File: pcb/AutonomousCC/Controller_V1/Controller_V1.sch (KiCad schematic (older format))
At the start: 7 parts, among them J1 Antenna_Conn_02x04_Odd_Even, U1 COM-09032, U2 Pico, U3 COM-09032

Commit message: Added USB Port, Button, LED
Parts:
- added D?: Red_LED, symbol Device:LED
- added D?: Green_LED, symbol Device:LED
- added J?: USB1130-15-A_REVA, GCT_USB1130-15-A_REVA, symbol USB1130-15-A_REVA:USB1130-15-A_REVA
- added R? (x2): 220_R_Small_US, symbol Device:R_Small_US
- added SW? (x2): SW_12mm_Push, Button_Switch_THT:SW_PUSH-12mm, symbol Switch:SW_Push
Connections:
- net +5V: now also J?.1 (VCC)
- net GND: now also J?.4 (GND)
- new net: J?.S1 (SHIELD), J?.S2 (SHIELD)
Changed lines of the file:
@@
 Wire Wire Line
 	6200 2550 6350 2550
+$Comp
+L USB1130-15-A_REVA:USB1130-15-A_REVA J?
+U 1 1 614FB04C
+P 9400 5550
+F 0 "J?" H 9630 5546 50  0000 L CNN
+F 1 "USB1130-15-A_REVA" H 9630 5455 50  0000 L CNN
+F 2 "GCT_USB1130-15-A_REVA" H 9400 5550 50  0001 L BNN
+F 3 "" H 9400 5550 50  0001 L BNN
+F 4 "A" H 9400 5550 50  0001 L BNN "PARTREV"
+F 5 "7.24mm" H 9400 5550 50  0001 L BNN "MAXIMUM_PACKAGE_HEIGHT"
+F 6 "Manufacturer Recommendations" H 9400 5550 50  0001 L BNN "STANDARD"
+F 7 "GCT" H 9400 5550 50  0001 L BNN "MANUFACTURER"
+	1    9400 5550
+	1    0    0    -1
+$EndComp
+$Comp
+L power:+5V #PWR?
+U 1 1 614FD28A
+P 8850 5350
+F 0 "#PWR?" H 8850 5200 50  0001 C CNN
+F 1 "+5V" V 8865 5478 50  0000 L CNN
+F 2 "" H 8850 5350 50  0001 C CNN
+F 3 "" H 8850 5350 50  0001 C CNN
+	1    8850 5350
+	0    -1   -1   0
+$EndComp
+$Comp
+L power:GND #PWR?
+U 1 1 615002B3
+P 8800 5650
+F 0 "#PWR?" H 8800 5400 50  0001 C CNN
+F 1 "GND" V 8805 5522 50  0000 R CNN
+F 2 "" H 8800 5650 50  0001 C CNN
+F 3 "" H 8800 5650 50  0001 C CNN
+	1    8800 5650
+	0    1    1    0
+$EndComp
+Wire Wire Line
+	8800 5650 9000 5650
+Wire Wire Line
+	8850 5350 9000 5350
+$Comp
+L Switch:SW_Push SW?
+U 1 1 6150A185
+P 3200 5700
+F 0 "SW?" H 3200 5985 50  0000 C CNN
+F 1 "SW_12mm_Push" H 3200 5894 50  0000 C CNN
+F 2 "Button_Switch_THT:SW_PUSH-12mm" H 3200 5900 50  0001 C CNN
+F 3 "~" H 3200 5900 50  0001 C CNN
+	1    3200 5700
+	1    0    0    -1
+$EndComp
+$Comp
+L Device:LED D?
+U 1 1 61515288
+P 4850 6100
+F 0 "D?" H 4843 6317 50  0000 C CNN
+F 1 "Red_LED" H 4843 6226 50  0000 C CNN
+F 2 "" H 4850 6100 50  0001 C CNN
+F 3 "~" H 4850 6100 50  0001 C CNN
+	1    4850 6100
+	1    0    0    -1
+$EndComp
+$Comp
+L Device:LED D?
+U 1 1 61517813
+P 3200 6100
+F 0 "D?" H 3193 6317 50  0000 C CNN
+F 1 "Green_LED" H 3193 6226 50  0000 C CNN
+F 2 "" H 3200 6100 50  0001 C CNN
+F 3 "~" H 3200 6100 50  0001 C CNN
+	1    3200 6100
+	1    0    0    -1
+$EndComp
+$Comp
+L Device:R_Small_US R?
+U 1 1 61518FD8
+P 3550 5900
+F 0 "R?" H 3618 5946 50  0000 L CNN
+F 1 "220_R_Small_US" H 3618 5855 50  0000 L CNN
+F 2 "" H 3550 5900 50  0001 C CNN
+F 3 "~" H 3550 5900 50  0001 C CNN
+	1    3550 5900
+	1    0    0    -1
+$EndComp
+$Comp
+L Device:R_Small_US R?
+U 1 1 61519A1B
+P 5250 5900
+F 0 "R?" H 5318 5946 50  0000 L CNN
+F 1 "220_R_Small_US" H 5318 5855 50  0000 L CNN
+F 2 "" H 5250 5900 50  0001 C CNN
+F 3 "~" H 5250 5900 50  0001 C CNN
+	1    5250 5900
+	1    0    0    -1
+$EndComp
+$Comp
+L Switch:SW_Push SW?
+U 1 1 6150B748
+P 4850 5700
+F 0 "SW?" H 4850 5985 50  0000 C CNN
+F 1 "SW_12mm_Push" H 4850 5894 50  0000 C CNN
+F 2 "Button_Switch_THT:SW_PUSH-12mm" H 4850 5900 50  0001 C CNN
+F 3 "~" H 4850 5900 50  0001 C CNN
+	1    4850 5700
+	1    0    0    -1
+$EndComp
 $EndSCHEMATC

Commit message: Updated Sch
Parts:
- removed D?: Red_LED, symbol Device:LED
- removed R?: 220_R_Small_US, symbol Device:R_Small_US
- added D2: RED_LED, symbol Device:LED
- added R2: 220_R_Small_US, symbol Device:R_Small_US
- gave numbers to parts that had none: 5
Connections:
- net GND: now also D1.1 (K), SW1.2, SW2.2, D2.1 (K)
- net GP09: now reaches U2.12 (GPIO9)
- net GP09: now also R2.2
- net GP10: now reaches U2.14 (GPIO10)
- net GP10: now also R1.2
- net GP15: now reaches U2.20 (GPIO15)
- net GP15: now also SW1.1
- net GP16: now reaches U2.21 (GPIO16)
- net GP16: now also SW2.1
- net at D1.2 (A): now also R1.1
- new net: D2.2 (A), R2.1
- no-connect marks 45 -> 41
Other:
- moved on the sheet: D1, R1, SW1, SW2
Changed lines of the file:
@@
 NoConn ~ 8300 3750
 NoConn ~ 8300 3650
-NoConn ~ 6200 4350
 NoConn ~ 6200 4150
 NoConn ~ 6200 4050
@@
 NoConn ~ 4800 3050
 NoConn ~ 4800 3450
-NoConn ~ 4800 3550
 NoConn ~ 4800 3650
-NoConn ~ 4800 3750
 NoConn ~ 4800 3850
 NoConn ~ 4800 3950
 NoConn ~ 4800 4050
 NoConn ~ 4800 4150
-NoConn ~ 4800 4350
 NoConn ~ 5400 4550
 NoConn ~ 5500 4550
@@
 	6200 2550 6350 2550
 $Comp
-L USB1130-15-A_REVA:USB1130-15-A_REVA J?
+L USB1130-15-A_REVA:USB1130-15-A_REVA J2
 U 1 1 614FB04C
 P 9400 5550
-F 0 "J?" H 9630 5546 50  0000 L CNN
+F 0 "J2" H 9630 5546 50  0000 L CNN
 F 1 "USB1130-15-A_REVA" H 9630 5455 50  0000 L CNN
 F 2 "GCT_USB1130-15-A_REVA" H 9400 5550 50  0001 L BNN
@@
 $EndComp
 $Comp
-L power:+5V #PWR?
+L power:+5V #PWR08
 U 1 1 614FD28A
 P 8850 5350
-F 0 "#PWR?" H 8850 5200 50  0001 C CNN
+F 0 "#PWR08" H 8850 5200 50  0001 C CNN
 F 1 "+5V" V 8865 5478 50  0000 L CNN
 F 2 "" H 8850 5350 50  0001 C CNN
@@
 $EndComp
 $Comp
-L power:GND #PWR?
+L power:GND #PWR07
 U 1 1 615002B3
 P 8800 5650
-F 0 "#PWR?" H 8800 5400 50  0001 C CNN
+F 0 "#PWR07" H 8800 5400 50  0001 C CNN
 F 1 "GND" V 8805 5522 50  0000 R CNN
 F 2 "" H 8800 5650 50  0001 C CNN
@@
 	8850 5350 9000 5350
 $Comp
-L Switch:SW_Push SW?
+L Switch:SW_Push SW1
 U 1 1 6150A185
-P 3200 5700
-F 0 "SW?" H 3200 5985 50  0000 C CNN
-F 1 "SW_12mm_Push" H 3200 5894 50  0000 C CNN
-F 2 "Button_Switch_THT:SW_PUSH-12mm" H 3200 5900 50  0001 C CNN
-F 3 "~" H 3200 5900 50  0001 C CNN
-	1    3200 5700
-	1    0    0    -1
-$EndComp
-$Comp
-L Device:LED D?
-U 1 1 61515288
-P 4850 6100
-F 0 "D?" H 4843 6317 50  0000 C CNN
-F 1 "Red_LED" H 4843 6226 50  0000 C CNN
-F 2 "" H 4850 6100 50  0001 C CNN
-F 3 "~" H 4850 6100 50  0001 C CNN
-	1    4850 6100
-	1    0    0    -1
-$EndComp
-$Comp
-L Device:LED D?
+P 2300 5450
+F 0 "SW1" H 2300 5735 50  0000 C CNN
+F 1 "SW_12mm_Push" H 2300 5644 50  0000 C CNN
+F 2 "Button_Switch_THT:SW_PUSH-12mm" H 2300 5650 50  0001 C CNN
+F 3 "~" H 2300 5650 50  0001 C CNN
+	1    2300 5450
+	1    0    0    -1
+$EndComp
+$Comp
+L Device:LED D1
 U 1 1 61517813
-P 3200 6100
-F 0 "D?" H 3193 6317 50  0000 C CNN
-F 1 "Green_LED" H 3193 6226 50  0000 C CNN
-F 2 "" H 3200 6100 50  0001 C CNN
-F 3 "~" H 3200 6100 50  0001 C CNN
-	1    3200 6100
-	1    0    0    -1
-$EndComp
-$Comp
-L Device:R_Small_US R?
+P 2300 6100
+F 0 "D1" H 2293 6317 50  0000 C CNN
+F 1 "Green_LED" H 2293 6226 50  0000 C CNN
+F 2 "" H 2300 6100 50  0001 C CNN
+F 3 "~" H 2300 6100 50  0001 C CNN
+	1    2300 6100
+	1    0    0    -1
+$EndComp
+$Comp
+L Switch:SW_Push SW2
+U 1 1 6150B748
+P 5050 5450
+F 0 "SW2" H 5050 5735 50  0000 C CNN
+F 1 "SW_12mm_Push" H 5050 5644 50  0000 C CNN
+F 2 "Button_Switch_THT:SW_PUSH-12mm" H 5050 5650 50  0001 C CNN
+F 3 "~" H 5050 5650 50  0001 C CNN
+	1    5050 5450
+	1    0    0    -1
+$EndComp
+$Comp
+L Device:R_Small_US R1
 U 1 1 61518FD8
-P 3550 5900
-F 0 "R?" H 3618 5946 50  0000 L CNN
-F 1 "220_R_Small_US" H 3618 5855 50  0000 L CNN
-F 2 "" H 3550 5900 50  0001 C CNN
-F 3 "~" H 3550 5900 50  0001 C CNN
-	1    3550 5900
-	1    0    0    -1
-$EndComp
-$Comp
-L Device:R_Small_US R?
-U 1 1 61519A1B
-P 5250 5900
-F 0 "R?" H 5318 5946 50  0000 L CNN
-F 1 "220_R_Small_US" H 5318 5855 50  0000 L CNN
-F 2 "" H 5250 5900 50  0001 C CNN
-F 3 "~" H 5250 5900 50  0001 C CNN
-	1    5250 5900
-	1    0    0    -1
-$EndComp
-$Comp
-L Switch:SW_Push SW?
-U 1 1 6150B748
-P 4850 5700
-F 0 "SW?" H 4850 5985 50  0000 C CNN
-F 1 "SW_12mm_Push" H 4850 5894 50  0000 C CNN
-F 2 "Button_Switch_THT:SW_PUSH-12mm" H 4850 5900 50  0001 C CNN
-F 3 "~" H 4850 5900 50  0001 C CNN
-	1    4850 5700
-	1    0    0    -1
-$EndComp
+P 2800 6100
+F 0 "R1" V 3000 6050 50  0000 L CNN
+F 1 "220_R_Small_US" V 2900 5750 50  0000 L CNN
+F 2 "" H 2800 6100 50  0001 C CNN
+F 3 "~" H 2800 6100 50  0001 C CNN
+	1    2800 6100
+	0    -1   -1   0
+$EndComp
+Text GLabel 3200 6100 2    50   Input ~ 0
+GP10
+$Comp
+L power:GND #PWR03
+U 1 1 61511AED
+P 1800 6100
+F 0 "#PWR03" H 1800 5850 50  0001 C CNN
+F 1 "GND" V 1805 5972 50  0000 R CNN
+F 2 "" H 1800 6100 50  0001 C CNN
+F 3 "" H 1800 6100 50  0001 C CNN
+	1    1800 6100
+	0    1    1    0
+$EndComp
+Wire Wire Line
+	1800 6100 2150 6100
+Wire Wire Line
+	2450 6100 2700 6100
+Wire Wire Line
+	2900 6100 3200 6100
+$Comp
+L Device:LED D2
+U 1 1 61517D52
+P 4900 6100
+F 0 "D2" H 4893 6317 50  0000 C CNN
+F 1 "RED_LED" H 4893 6226 50  0000 C CNN
+F 2 "" H 4900 6100 50  0001 C CNN
+F 3 "~" H 4900 6100 50  0001 C CNN
+	1    4900 6100
+	1    0    0    -1
+$EndComp
+$Comp
+L Device:R_Small_US R2
+U 1 1 61517D58
+P 5400 6100
+F 0 "R2" V 5600 6050 50  0000 L CNN
+F 1 "220_R_Small_US" V 5500 5750 50  0000 L CNN
+F 2 "" H 5400 6100 50  0001 C CNN
+F 3 "~" H 5400 6100 50  0001 C CNN
+	1    5400 6100
+	0    -1   -1   0
+$EndComp
+Text GLabel 5800 6100 2    50   Input ~ 0
+GP09
+$Comp
+L power:GND #PWR05
+U 1 1 61517D5F
+P 4400 6100
+F 0 "#PWR05" H 4400 5850 50  0001 C CNN
+F 1 "GND" V 4405 5972 50  0000 R CNN
+F 2 "" H 4400 6100 50  0001 C CNN
+F 3 "" H 4400 6100 50  0001 C CNN
+	1    4400 6100
+	0    1    1    0
+$EndComp
+Wire Wire Line
+	4400 6100 4750 6100
+Wire Wire Line
+	5050 6100 5300 6100
+Wire Wire Line
+	5500 6100 5800 6100
+$Comp
+L power:GND #PWR04
+U 1 1 6151B378
+P 2750 5450
+F 0 "#PWR04" H 2750 5200 50  0001 C CNN
+F 1 "GND" V 2755 5322 50  0000 R CNN
+F 2 "" H 2750 5450 50  0001 C CNN
+F 3 "" H 2750 5450 50  0001 C CNN
+	1    2750 5450
+	0    -1   -1   0
+$EndComp
+$Comp
+L power:GND #PWR06
+U 1 1 6151BF18
+P 5500 5450
+F 0 "#PWR06" H 5500 5200 50  0001 C CNN
+F 1 "GND" V 5505 5322 50  0000 R CNN
+F 2 "" H 5500 5450 50  0001 C CNN
+F 3 "" H 5500 5450 50  0001 C CNN
+	1    5500 5450
+	0    -1   -1   0
+$EndComp
+Text GLabel 4650 3550 0    50   Input ~ 0
+GP09
+Text GLabel 4650 3750 0    50   Input ~ 0
+GP10
+Wire Wire Line
+	5500 5450 5250 5450
+Wire Wire Line
+	2750 5450 2500 5450
+Text GLabel 1800 5450 0    50   Input ~ 0
+GP15
+Text GLabel 4500 5450 0    50   Input ~ 0
+GP16
+Wire Wire Line
+	4500 5450 4850 5450
+Wire Wire Line
+	1800 5450 2100 5450
+Text GLabel 6350 4350 2    50   Input ~ 0
+GP16
+Text GLabel 4650 4350 0    50   Input ~ 0
+GP15
+Wire Wire Line
+	4650 4350 4800 4350
+Wire Wire Line
+	6350 4350 6200 4350
+Wire Wire Line
+	4650 3750 4800 3750
+Wire Wire Line
+	4800 3550 4650 3550
 $EndSCHEMATC

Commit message: Autosave
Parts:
- D1, D2: footprint (none) -> LED_THT:LED_D3.0mm
- R1, R2: footprint (none) -> Resistor_THT:R_Axial_DIN0204_L3.6mm_D1.6mm_P7.62mm_Horizontal
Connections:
- no-connect marks 41 -> 44
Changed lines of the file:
@@
 F 0 "D1" H 2293 6317 50  0000 C CNN
 F 1 "Green_LED" H 2293 6226 50  0000 C CNN
-F 2 "" H 2300 6100 50  0001 C CNN
+F 2 "LED_THT:LED_D3.0mm" H 2300 6100 50  0001 C CNN
 F 3 "~" H 2300 6100 50  0001 C CNN
 	1    2300 6100
@@
 F 0 "R1" V 3000 6050 50  0000 L CNN
 F 1 "220_R_Small_US" V 2900 5750 50  0000 L CNN
-F 2 "" H 2800 6100 50  0001 C CNN
+F 2 "Resistor_THT:R_Axial_DIN0204_L3.6mm_D1.6mm_P7.62mm_Horizontal" H 2800 6100 50  0001 C CNN
 F 3 "~" H 2800 6100 50  0001 C CNN
 	1    2800 6100
@@
 F 0 "D2" H 4893 6317 50  0000 C CNN
 F 1 "RED_LED" H 4893 6226 50  0000 C CNN
-F 2 "" H 4900 6100 50  0001 C CNN
+F 2 "LED_THT:LED_D3.0mm" H 4900 6100 50  0001 C CNN
 F 3 "~" H 4900 6100 50  0001 C CNN
 	1    4900 6100
@@
 F 0 "R2" V 5600 6050 50  0000 L CNN
 F 1 "220_R_Small_US" V 5500 5750 50  0000 L CNN
-F 2 "" H 5400 6100 50  0001 C CNN
+F 2 "Resistor_THT:R_Axial_DIN0204_L3.6mm_D1.6mm_P7.62mm_Horizontal" H 5400 6100 50  0001 C CNN
 F 3 "~" H 5400 6100 50  0001 C CNN
 	1    5400 6100
@@
 Wire Wire Line
 	4800 3550 4650 3550
+NoConn ~ 9000 5450
+NoConn ~ 9000 5550
+NoConn ~ 9000 5850
 $EndSCHEMATC

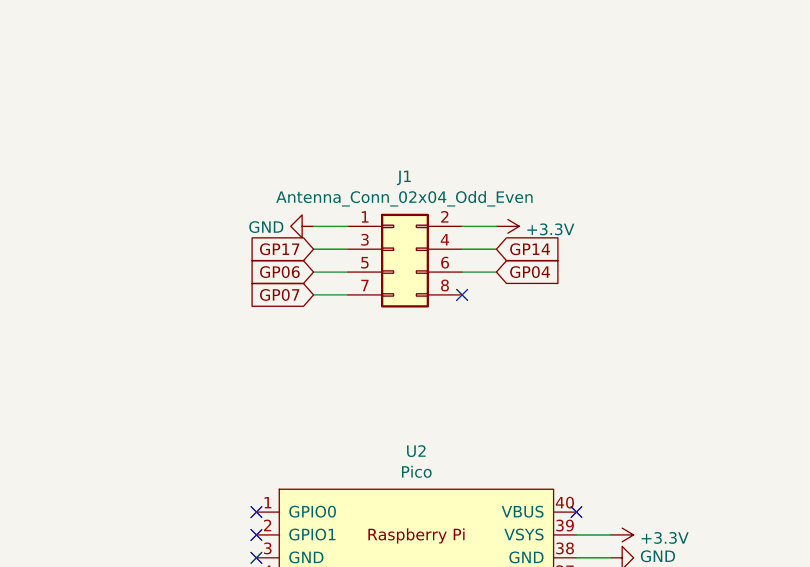
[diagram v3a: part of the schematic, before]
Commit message: Update Controller Antenna Pins
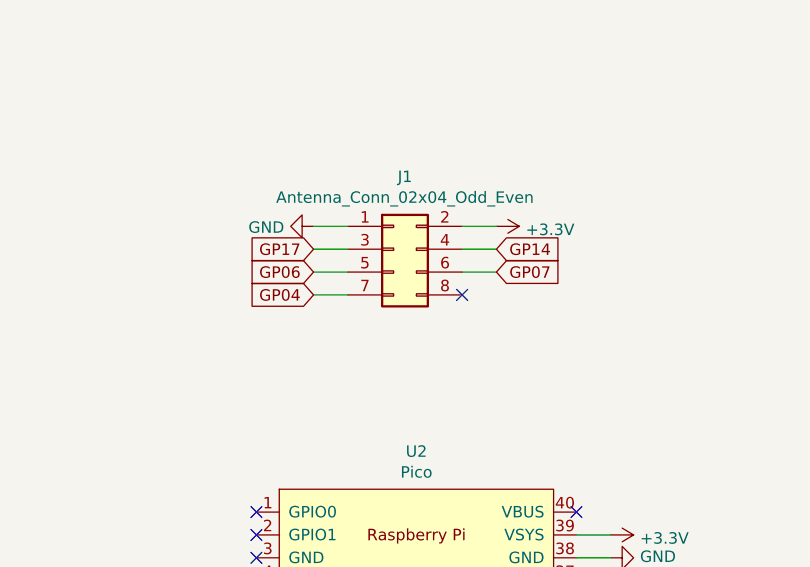
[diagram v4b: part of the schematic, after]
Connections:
- net GP04: now also J1.7 (Pin_7); no longer J1.6 (Pin_6)
- net GP07: now also J1.6 (Pin_6); no longer J1.7 (Pin_7)
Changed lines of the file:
@@
 Text GLabel 5050 1300 0    50   Input ~ 0
 GP17
-Text GLabel 5050 1500 0    50   Input ~ 0
+Text GLabel 5850 1400 2    50   Input ~ 0
 GP07
 Text GLabel 5850 1300 2    50   Input ~ 0
@@
 NoConn ~ 5700 1500
 Wire Wire Line
-	5700 1400 5850 1400
+	5200 1500 5050 1500
 Wire Wire Line
 	5700 1300 5850 1300
@@
 	5200 1400 5050 1400
 Wire Wire Line
-	5050 1500 5200 1500
+	5850 1400 5700 1400
 $Comp
 L power:GND #PWR0102
@@
 Text GLabel 6350 3350 2    50   Input ~ 0
 GP26
-Text GLabel 5850 1400 2    50   Input ~ 0
+Text GLabel 5050 1500 0    50   Input ~ 0
 GP04
 Text GLabel 4650 2950 0    50   Input ~ 0

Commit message: CC Controller and Brain VERSION 1.1
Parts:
- added H1, H2, H3, H4: MountingHole, MountingHole:MountingHole_2.2mm_M2_Pad, symbol Mechanical:MountingHole
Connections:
- net +3V3: now also SW1.2, SW2.2, U2.36 (3V3); no longer C2.1, J1.2 (Pin_2), U2.39 (VSYS), VR1.2 (OUTPUT)
- net GND: no longer SW1.2, SW2.2
- new net +3.3VA: C2.1, J1.2 (Pin_2), U2.39 (VSYS), VR1.2 (OUTPUT)
- no-connect marks 44 -> 43
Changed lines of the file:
@@
 	1    0    0    -1
-$EndComp
-$Comp
-L power:+3.3V #PWR0101
-U 1 1 614D5BB9
-P 5850 1200
-F 0 "#PWR0101" H 5850 1050 50  0001 C CNN
-F 1 "+3.3V" V 5865 1328 50  0000 L CNN
-F 2 "" H 5850 1200 50  0001 C CNN
-F 3 "" H 5850 1200 50  0001 C CNN
-	1    5850 1200
-	0    1    1    0
 $EndComp
 Text GLabel 5050 1300 0    50   Input ~ 0
@@
 $EndComp
 $Comp
-L power:+3.3V #PWR0110
-U 1 1 61510D22
-P 10300 1250
-F 0 "#PWR0110" H 10300 1100 50  0001 C CNN
-F 1 "+3.3V" V 10300 1350 50  0000 L CNN
-F 2 "" H 10300 1250 50  0001 C CNN
-F 3 "" H 10300 1250 50  0001 C CNN
-	1    10300 1250
-	0    1    1    0
-$EndComp
-$Comp
 L power:GND #PWR0111
 U 1 1 61511661
@@
 NoConn ~ 6200 3150
 NoConn ~ 6200 2950
-NoConn ~ 6200 2850
 NoConn ~ 6200 2750
 NoConn ~ 6200 2450
@@
 NoConn ~ 10400 -550
 $Comp
-L power:+3.3V #PWR01
-U 1 1 6153A302
-P 6350 2550
-F 0 "#PWR01" H 6350 2400 50  0001 C CNN
-F 1 "+3.3V" V 6365 2678 50  0000 L CNN
-F 2 "" H 6350 2550 50  0001 C CNN
-F 3 "" H 6350 2550 50  0001 C CNN
-	1    6350 2550
-	0    1    1    0
-$EndComp
-$Comp
 L power:GND #PWR02
 U 1 1 6153A693
@@
 Wire Wire Line
 	5500 6100 5800 6100
-$Comp
-L power:GND #PWR04
-U 1 1 6151B378
-P 2750 5450
-F 0 "#PWR04" H 2750 5200 50  0001 C CNN
-F 1 "GND" V 2755 5322 50  0000 R CNN
-F 2 "" H 2750 5450 50  0001 C CNN
-F 3 "" H 2750 5450 50  0001 C CNN
-	1    2750 5450
-	0    -1   -1   0
-$EndComp
-$Comp
-L power:GND #PWR06
-U 1 1 6151BF18
-P 5500 5450
-F 0 "#PWR06" H 5500 5200 50  0001 C CNN
-F 1 "GND" V 5505 5322 50  0000 R CNN
-F 2 "" H 5500 5450 50  0001 C CNN
-F 3 "" H 5500 5450 50  0001 C CNN
-	1    5500 5450
-	0    -1   -1   0
-$EndComp
 Text GLabel 4650 3550 0    50   Input ~ 0
 GP09
 Text GLabel 4650 3750 0    50   Input ~ 0
 GP10
-Wire Wire Line
-	5500 5450 5250 5450
-Wire Wire Line
-	2750 5450 2500 5450
 Text GLabel 1800 5450 0    50   Input ~ 0
 GP15
@@
 NoConn ~ 9000 5550
 NoConn ~ 9000 5850
+$Comp
+L power:+3.3VA #PWR0101
+U 1 1 616B9148
+P 6350 2550
+F 0 "#PWR0101" H 6350 2400 50  0001 C CNN
+F 1 "+3.3VA" V 6365 2678 50  0000 L CNN
+F 2 "" H 6350 2550 50  0001 C CNN
+F 3 "" H 6350 2550 50  0001 C CNN
+	1    6350 2550
+	0    1    1    0
+$EndComp
+$Comp
+L power:+3.3V #PWR0112
+U 1 1 616BB474
+P 6400 2850
+F 0 "#PWR0112" H 6400 2700 50  0001 C CNN
+F 1 "+3.3V" V 6415 2978 50  0000 L CNN
+F 2 "" H 6400 2850 50  0001 C CNN
+F 3 "" H 6400 2850 50  0001 C CNN
+	1    6400 2850
+	0    1    1    0
+$EndComp
+Wire Wire Line
+	6200 2850 6400 2850
+$Comp
+L power:+3.3VA #PWR0113
+U 1 1 616C0192
+P 5850 1200
+F 0 "#PWR0113" H 5850 1050 50  0001 C CNN
+F 1 "+3.3VA" V 5865 1328 50  0000 L CNN
+F 2 "" H 5850 1200 50  0001 C CNN
+F 3 "" H 5850 1200 50  0001 C CNN
+	1    5850 1200
+	0    1    1    0
+$EndComp
+$Comp
+L power:+3.3VA #PWR01
+U 1 1 616C36FD
+P 10300 1250
+F 0 "#PWR01" H 10300 1100 50  0001 C CNN
+F 1 "+3.3VA" V 10315 1378 50  0000 L CNN
+F 2 "" H 10300 1250 50  0001 C CNN
+F 3 "" H 10300 1250 50  0001 C CNN
+	1    10300 1250
+	0    1    1    0
+$EndComp
+$Comp
+L power:+3.3V #PWR0110
+U 1 1 616D6DE7
+P 2700 5450
+F 0 "#PWR0110" H 2700 5300 50  0001 C CNN
+F 1 "+3.3V" V 2715 5578 50  0000 L CNN
+F 2 "" H 2700 5450 50  0001 C CNN
+F 3 "" H 2700 5450 50  0001 C CNN
+	1    2700 5450
+	0    1    1    0
+$EndComp
+Wire Wire Line
+	2500 5450 2700 5450
+$Comp
+L power:+3.3V #PWR0114
+U 1 1 616DEE5A
+P 5500 5450
+F 0 "#PWR0114" H 5500 5300 50  0001 C CNN
+F 1 "+3.3V" V 5515 5578 50  0000 L CNN
+F 2 "" H 5500 5450 50  0001 C CNN
+F 3 "" H 5500 5450 50  0001 C CNN
+	1    5500 5450
+	0    1    1    0
+$EndComp
+Wire Wire Line
+	5250 5450 5500 5450
+$Comp
+L Mechanical:MountingHole H2
+U 1 1 616E6AD8
+P 2050 1300
+F 0 "H2" H 2150 1346 50  0000 L CNN
+F 1 "MountingHole" H 2150 1255 50  0000 L CNN
+F 2 "MountingHole:MountingHole_2.2mm_M2_Pad" H 2050 1300 50  0001 C CNN
+F 3 "~" H 2050 1300 50  0001 C CNN
+	1    2050 1300
+	1    0    0    -1
+$EndComp
+$Comp
+L Mechanical:MountingHole H3
+U 1 1 616E70BF
+P 2050 1550
+F 0 "H3" H 2150 1596 50  0000 L CNN
+F 1 "MountingHole" H 2150 1505 50  0000 L CNN
+F 2 "MountingHole:MountingHole_2.2mm_M2_Pad" H 2050 1550 50  0001 C CNN
+F 3 "~" H 2050 1550 50  0001 C CNN
+	1    2050 1550
+	1    0    0    -1
+$EndComp
+$Comp
+L Mechanical:MountingHole H4
+U 1 1 616E75A2
+P 2050 1800
+F 0 "H4" H 2150 1846 50  0000 L CNN
+F 1 "MountingHole" H 2150 1755 50  0000 L CNN
+F 2 "MountingHole:MountingHole_2.2mm_M2_Pad" H 2050 1800 50  0001 C CNN
+F 3 "~" H 2050 1800 50  0001 C CNN
+	1    2050 1800
+	1    0    0    -1
+$EndComp
+$Comp
+L Mechanical:MountingHole H1
+U 1 1 616E5E70
+P 2050 1050
+F 0 "H1" H 2150 1096 50  0000 L CNN
+F 1 "MountingHole" H 2150 1005 50  0000 L CNN
+F 2 "MountingHole:MountingHole_2.2mm_M2_Pad" H 2050 1050 50  0001 C CNN
+F 3 "~" H 2050 1050 50  0001 C CNN
+	1    2050 1050
+	1    0    0    -1
+$EndComp
 $EndSCHEMATC
